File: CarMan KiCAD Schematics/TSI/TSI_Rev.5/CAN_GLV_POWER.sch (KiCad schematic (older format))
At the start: 49 parts, among them J31 Cooling Jumper, K2 G5LE-1-E, K3 SFS2-DC24V, K4 SFS2-DC24V, Q11 TN2130K1-G, U14 Bottom Left, U15 Top Left, U17 Top Right, U2 Bottom Right, U20 TLP293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

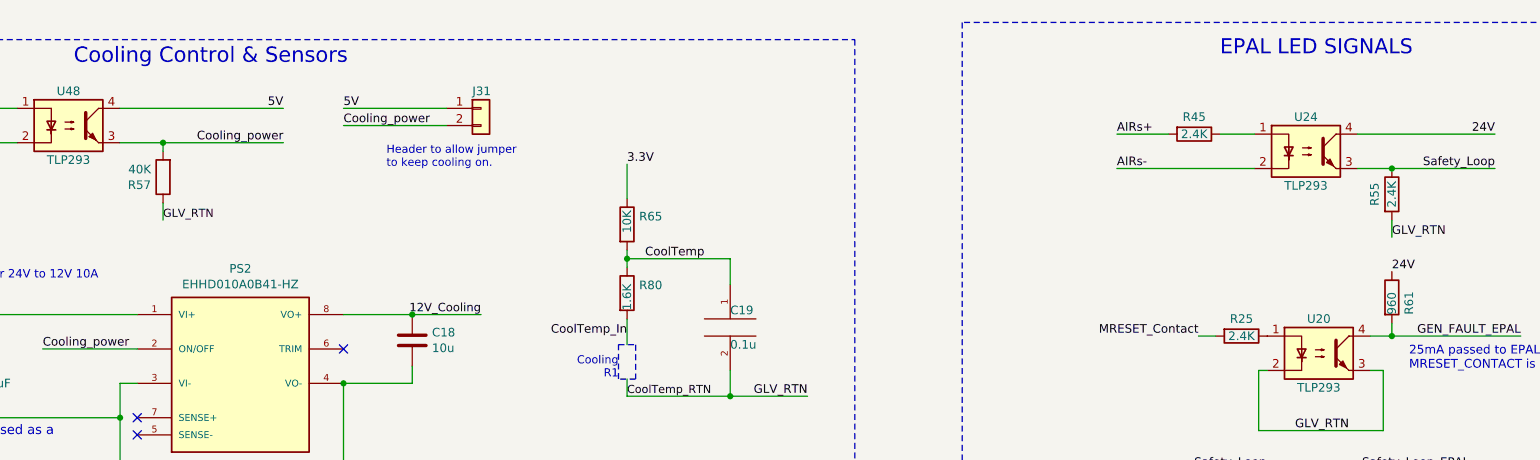
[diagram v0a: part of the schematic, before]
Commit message: TSI Updated & error fixes: added pull down resistors, and 5V_ISO_RTN
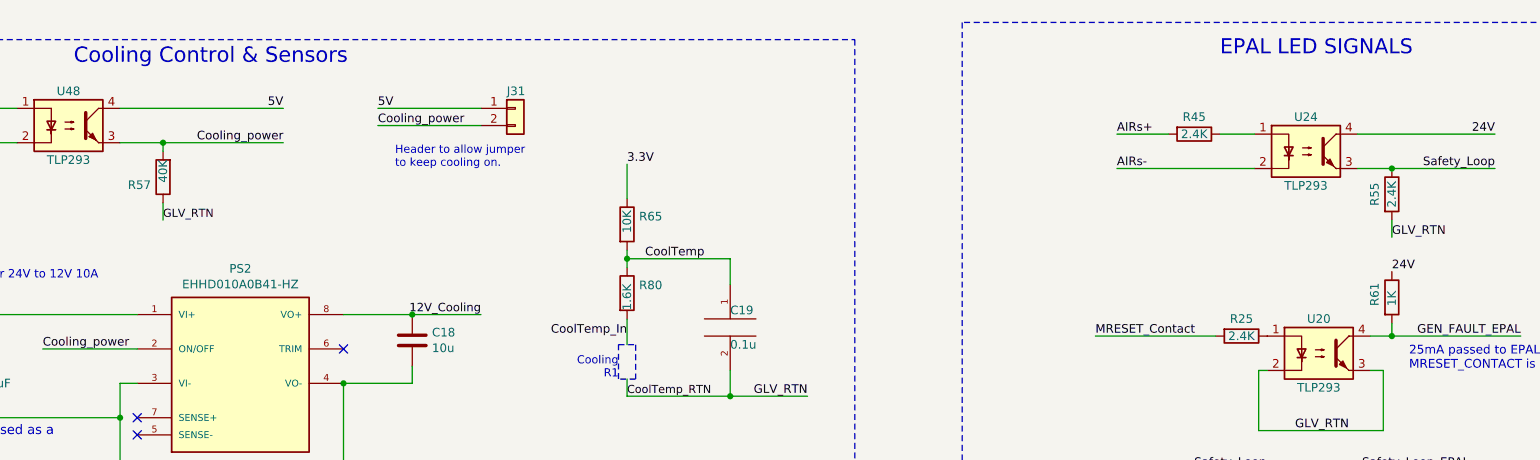
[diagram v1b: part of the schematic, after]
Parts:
- R61: value 960 -> 1K
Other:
- moved on the sheet: J31
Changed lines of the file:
@@
 P 5200 1450
 F 0 "R57" H 5270 1496 50  0000 L CNN
-F 1 "40K" H 5270 1405 50  0000 L CNN
+F 1 "40K" V 5200 1350 50  0000 L CNN
 F 2 "Resistor_SMD:R_0805_2012Metric_Pad1.15x1.40mm_HandSolder" V 5130 1450 50  0001 C CNN
 F 3 "~" H 5200 1450 50  0001 C CNN
@@
 Wire Notes Line
 	2950 650  2950 3250
-Text Label 11225 2375 2    50   ~ 0
+Text Label 10625 2375 0    50   ~ 0
 MRESET_Contact
 Text HLabel 14950 3875 0    50   Input ~ 0
@@
 $EndComp
 Wire Wire Line
-	11325 2375 11225 2375
-Wire Wire Line
 	12225 2575 12300 2575
 Text Label 12100 2925 2    50   ~ 0
@@
 L Connector_Generic:Conn_01x02 J?
 U 1 1 601DA5ED
-P 7050 1050
+P 7250 1050
 AR Path="/601DA5ED" Ref="J?"  Part="1"
 AR Path="/5FE1DE7D/601DA5ED" Ref="J31"  Part="1"
-F 0 "J31" H 7000 1150 50  0000 L CNN
-F 1 "Cooling Jumper" H 7000 1150 50  0001 L CNN
-F 2 "Connector_PinSocket_2.54mm:PinSocket_1x02_P2.54mm_Vertical" H 7050 1050 50  0001 C CNN
-F 3 "~" H 7050 1050 50  0001 C CNN
-	1    7050 1050
-	1    0    0    -1
-$EndComp
-Text Notes 6500 1400 0    47   ~ 0
+F 0 "J31" H 7200 1150 50  0000 L CNN
+F 1 "Cooling Jumper" H 7200 1150 50  0001 L CNN
+F 2 "Connector_PinSocket_2.54mm:PinSocket_1x02_P2.54mm_Vertical" H 7250 1050 50  0001 C CNN
+F 3 "~" H 7250 1050 50  0001 C CNN
+	1    7250 1050
+	1    0    0    -1
+$EndComp
+Text Notes 6550 1400 0    47   ~ 0
 Header to allow jumper \nto keep cooling on.\n
-Text Label 6250 1150 0    50   ~ 0
+Text Label 6450 1150 0    50   ~ 0
 Cooling_power
 Wire Wire Line
-	6250 1150 6850 1150
-Wire Wire Line
-	6250 1050 6850 1050
-Text Label 6250 1050 0    50   ~ 0
+	6450 1150 7050 1150
+Wire Wire Line
+	6450 1050 7050 1050
+Text Label 6450 1050 0    50   ~ 0
 5V
 $Comp
@@
 U 1 1 601328F4
 P 12350 2150
-F 0 "R61" V 12450 2050 50  0000 L CNN
-F 1 "960" V 12350 2050 50  0000 L CNN
+F 0 "R61" V 12250 2100 50  0000 L CNN
+F 1 "1K" V 12350 2100 50  0000 L CNN
 F 2 "Resistor_SMD:R_0805_2012Metric_Pad1.15x1.40mm_HandSolder" V 12280 2150 50  0001 C CNN
 F 3 "~" H 12350 2150 50  0001 C CNN
@@
 Wire Notes Line
 	9750 9950 9750 10075
+Wire Wire Line
+	10625 2375 11325 2375
 $EndSCHEMATC

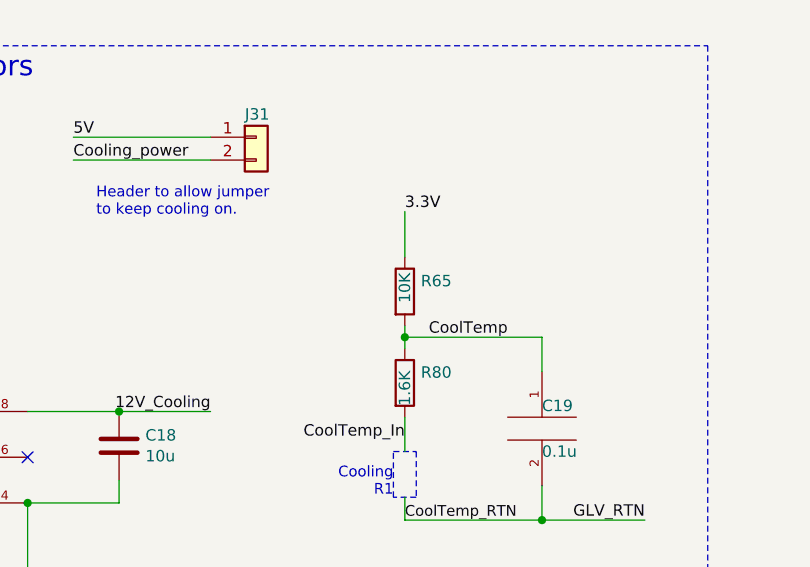
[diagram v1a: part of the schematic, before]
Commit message: ADDED K1-APAN3105 Relay to symbol and footprint libraries
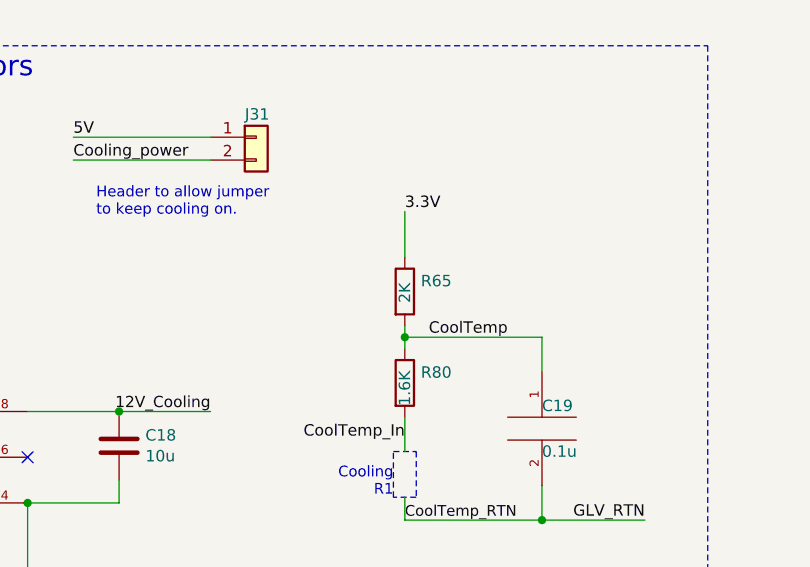
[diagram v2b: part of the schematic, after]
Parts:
- R65: value 10K -> 2K
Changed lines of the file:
@@
 AR Path="/5FE1DE7D/608CA5C5" Ref="R65"  Part="1"
 F 0 "R65" H 7970 1771 50  0000 L CNN
-F 1 "10K" V 7900 1675 50  0000 L CNN
+F 1 "2K" V 7900 1675 50  0000 L CNN
 F 2 "Resistor_SMD:R_0805_2012Metric_Pad1.15x1.40mm_HandSolder" V 7830 1725 50  0001 C CNN
 F 3 "~" H 7900 1725 50  0001 C CNN

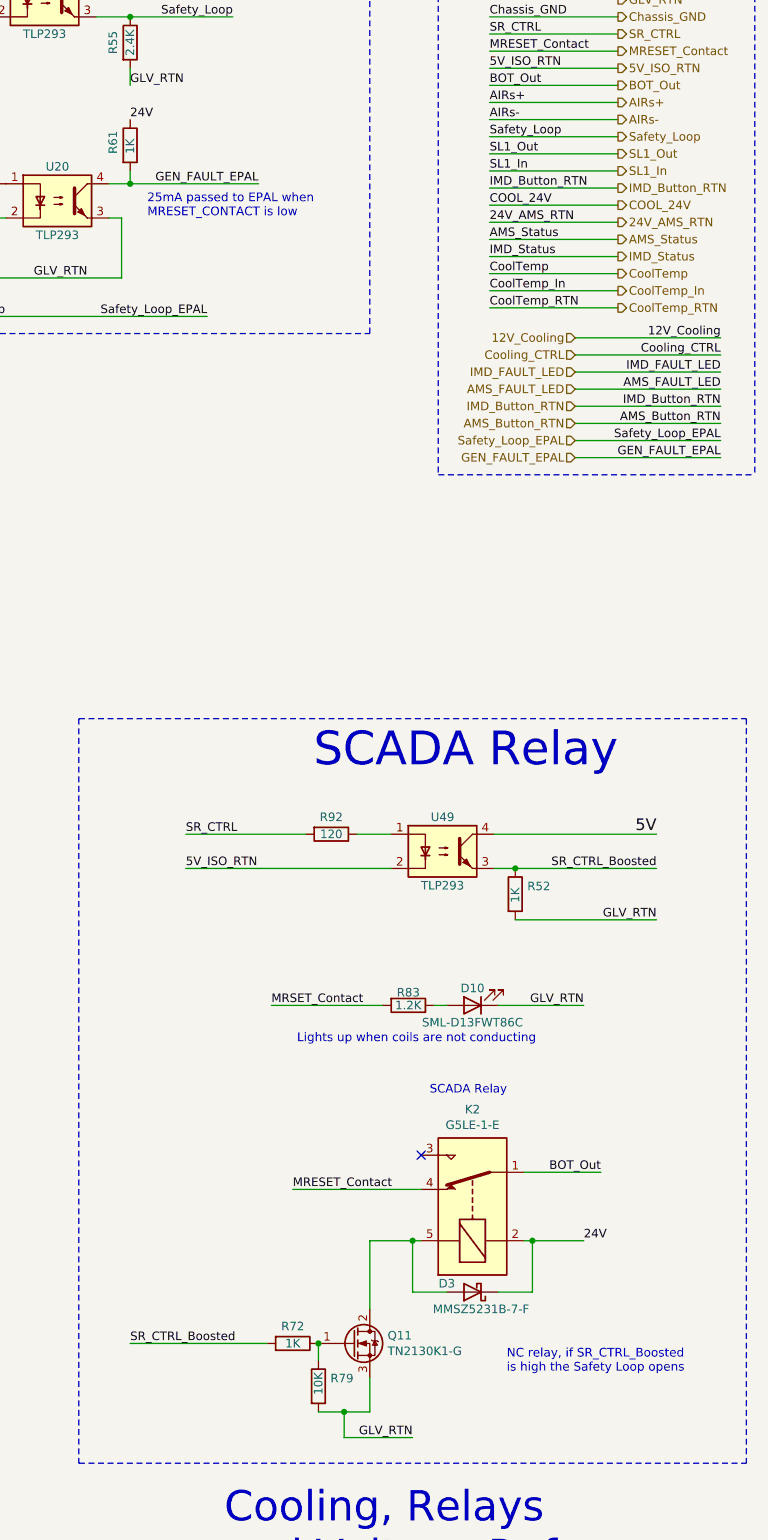
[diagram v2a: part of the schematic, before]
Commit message: - removed testing headers (All pins were easily testable, one that weren't received testing points) - Added pull up resistor at drain of SCADA Relay - Fixed issue with U27-PC_Ready signal not being isolated, also added pull down resistor. Comment about 5V_ISO from logic is necessary - Increased Resistor values across D1 and D4 to cut intensity - Updated PCB board with Netlist
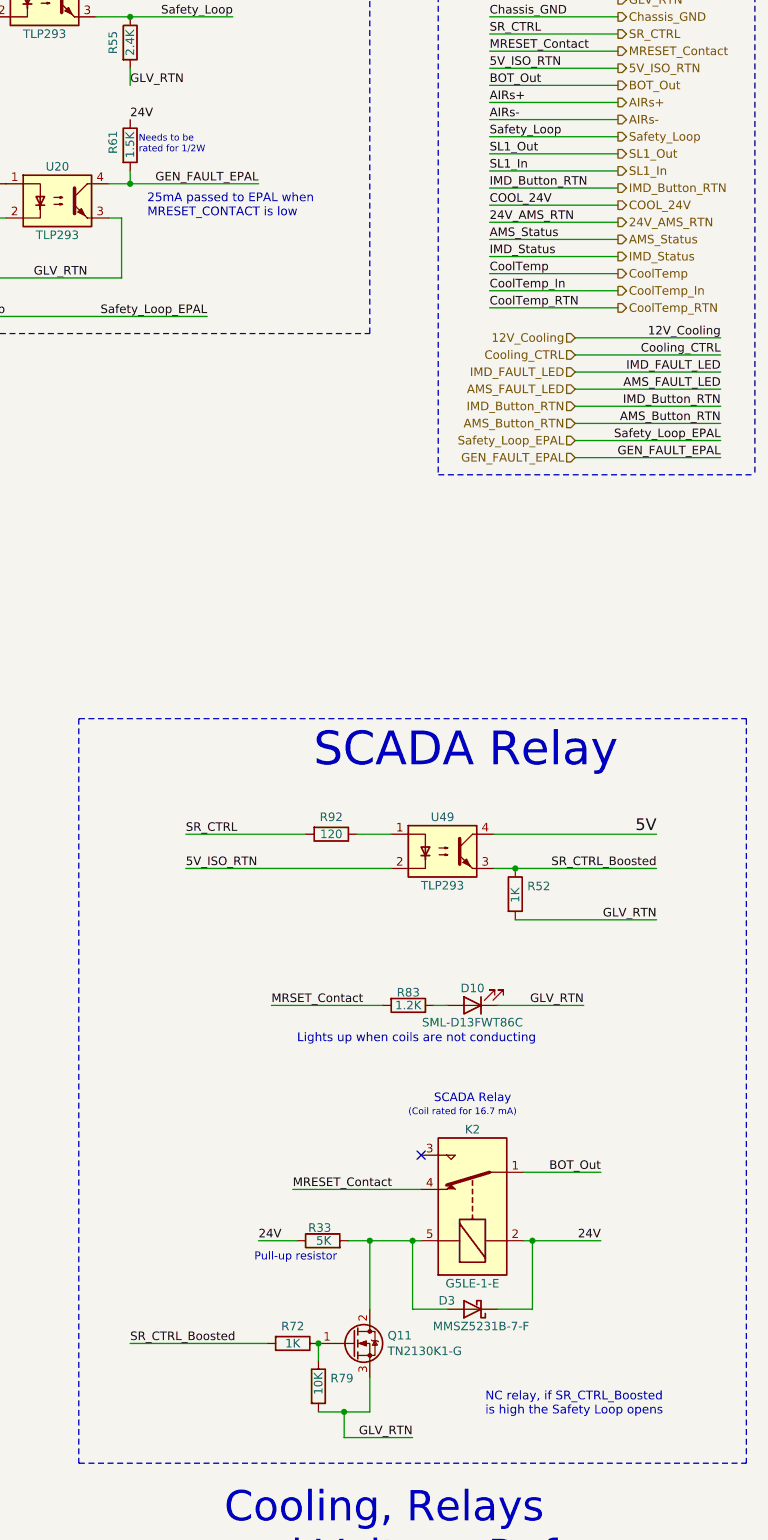
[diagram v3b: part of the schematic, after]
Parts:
- added R33: 5K, Resistor_SMD:R_0805_2012Metric_Pad1.15x1.40mm_HandSolder, symbol Device:R
- R61: value 1K -> 1.5K
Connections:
- wire segments 198 -> 200
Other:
- note added: "(Coil rated for 16.7 mA)"
- note added: "Needs to be\nrated for 1/2W\n"
- note added: "Pull-up resistor"
- moved on the sheet: D3
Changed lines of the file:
@@
 L Device:D_Schottky D3
 U 1 1 5FB8F043
-P 14350 8850
-F 0 "D3" H 14500 8800 50  0000 C CNN
-F 1 "MMSZ5231B-7-F" H 14300 8950 50  0000 C CNN
-F 2 "Diode_SMD:D_SOD-123" H 14350 8850 50  0001 C CNN
-F 3 "~" H 14350 8850 50  0001 C CNN
-	1    14350 8850
+P 14350 8950
+F 0 "D3" H 14500 8900 50  0000 C CNN
+F 1 "MMSZ5231B-7-F" H 14300 9050 50  0000 C CNN
+F 2 "Diode_SMD:D_SOD-123" H 14350 8950 50  0001 C CNN
+F 3 "~" H 14350 8950 50  0001 C CNN
+	1    14350 8950
 	-1   0    0    1
 $EndComp
@@
 	0    1    1    0
 $EndComp
-Text Notes 14100 7700 0    50   ~ 0
+Text Notes 14125 7750 0    50   ~ 0
 SCADA Relay\n
 $Comp
@@
 Cooling Control & Sensors\n
 $Comp
-L Device:R R79
-U 1 1 5FB66337
-P 13450 9400
-F 0 "R79" H 13520 9446 50  0000 L CNN
-F 1 "10K" V 13450 9350 50  0000 L CNN
-F 2 "Resistor_SMD:R_0805_2012Metric_Pad1.15x1.40mm_HandSolder" V 13380 9400 50  0001 C CNN
-F 3 "~" H 13450 9400 50  0001 C CNN
-	1    13450 9400
-	1    0    0    -1
-$EndComp
-$Comp
 L Device:R R72
 U 1 1 5FB6696B
@@
 Wire Wire Line
 	13750 8550 14000 8550
-Text Label 15000 8550 0    50   ~ 0
+Text Label 15100 8550 2    50   ~ 0
 24V
 Wire Wire Line
-	14500 8850 14700 8850
-Wire Wire Line
-	14700 8850 14700 8550
+	14500 8950 14700 8950
 Connection ~ 14700 8550
 Wire Wire Line
-	14700 8550 15000 8550
-Wire Wire Line
-	14200 8850 14000 8850
-Wire Wire Line
-	14000 8850 14000 8550
+	14200 8950 14000 8950
 Connection ~ 14000 8550
 Wire Wire Line
@@
 AR Path="/5FB466B1" Ref="RL?"  Part="1"
 AR Path="/5FE1DE7D/5FB466B1" Ref="K2"  Part="1"
-F 0 "K2" V 14917 8350 50  0000 C CNN
-F 1 "G5LE-1-E" V 14826 8350 50  0000 C CNN
+F 0 "K2" V 14800 8350 50  0000 C CNN
+F 1 "G5LE-1-E" V 13900 8350 50  0000 C CNN
 F 2 "TSI_Rev_2021_Footprint_Lib:G5LE-1-E DC24" H 14600 8950 50  0001 C CNN
 F 3 "https://media.digikey.com/pdf/Data%20Sheets/Omron%20PDFs/G5LE-E_G.pdf" H 14600 8950 50  0001 C CNN
@@
 P 12350 2150
 F 0 "R61" V 12250 2100 50  0000 L CNN
-F 1 "1K" V 12350 2100 50  0000 L CNN
+F 1 "1.5K" V 12350 2075 50  0000 L CNN
 F 2 "Resistor_SMD:R_0805_2012Metric_Pad1.15x1.40mm_HandSolder" V 12280 2150 50  0001 C CNN
 F 3 "~" H 12350 2150 50  0001 C CNN
@@
 Wire Wire Line
 	14125 7175 14200 7175
-Text Notes 14550 9325 0    51   ~ 0
+Text Notes 14425 9575 0    51   ~ 0
 NC relay, if SR_CTRL_Boosted \nis high the Safety Loop opens
 Text Label 7900 1375 0    50   ~ 0
@@
 Wire Wire Line
 	10625 2375 11325 2375
+$Comp
+L Device:R R79
+U 1 1 5FB66337
+P 13450 9400
+F 0 "R79" H 13520 9446 50  0000 L CNN
+F 1 "10K" V 13450 9350 50  0000 L CNN
+F 2 "Resistor_SMD:R_0805_2012Metric_Pad1.15x1.40mm_HandSolder" V 13380 9400 50  0001 C CNN
+F 3 "~" H 13450 9400 50  0001 C CNN
+	1    13450 9400
+	1    0    0    -1
+$EndComp
+$Comp
+L Device:R R33
+U 1 1 6090AD09
+P 13475 8550
+F 0 "R33" V 13550 8500 50  0000 L CNN
+F 1 "5K" V 13475 8500 50  0000 L CNN
+F 2 "Resistor_SMD:R_0805_2012Metric_Pad1.15x1.40mm_HandSolder" V 13405 8550 50  0001 C CNN
+F 3 "~" H 13475 8550 50  0001 C CNN
+	1    13475 8550
+	0    -1   -1   0
+$EndComp
+Wire Wire Line
+	13750 8550 13625 8550
+Connection ~ 13750 8550
+Wire Wire Line
+	13100 8550 13325 8550
+Text Label 13100 8550 0    50   ~ 0
+24V
+Text Notes 13075 8675 0    47   ~ 0
+Pull-up resistor
+Text Notes 13975 7825 0    39   ~ 0
+(Coil rated for 16.7 mA)
+Wire Wire Line
+	14700 8550 14700 8950
+Wire Wire Line
+	14000 8550 14000 8950
+Wire Wire Line
+	14700 8550 15100 8550
+Text Notes 12400 2200 0    39   ~ 0
+Needs to be\nrated for 1/2W\n
 $EndSCHEMATC
